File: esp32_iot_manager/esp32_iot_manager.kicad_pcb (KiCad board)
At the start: 4 copper layers, 76.5 x 58 mm, 88 parts, among them J1 SS-52400-002, J2 B2B-PH-SM4-TB, J3 GSD090012SEU, J4 Conn_01x04_Pin, J5 Conn_01x05_Pin, Q1 TEMT6000X01, Q2 BC817, Q3 BC817, U1 MCP73871, U2 BME280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

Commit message: 4 layer pcb design done
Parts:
- moved LED4 7.12 mm to (160.0, 54.9)
- moved R10 7.12 mm to (160.0, 51.1)
- moved U5 4.82 mm to (171.2, 58.3)
- moved C11 4.54 mm to (170.5, 55.1)
- moved R12 4.54 mm to (168.2, 56.9)
- moved R13 4.54 mm to (168.2, 53.3)
- moved TP1 2.50 mm to (193.0, 62.5)
- moved TP2 1.52 mm to (193.0, 66.5)
- moved TP5 1.50 mm to (193.0, 78.2)
- moved TP3 0.75 mm to (193.0, 70.5)
- moved TP4 0.50 mm to (193.0, 74.5)
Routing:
- added copper zone on In1.Cu, net 3.3V
- added copper zone on In2.Cu, net GND

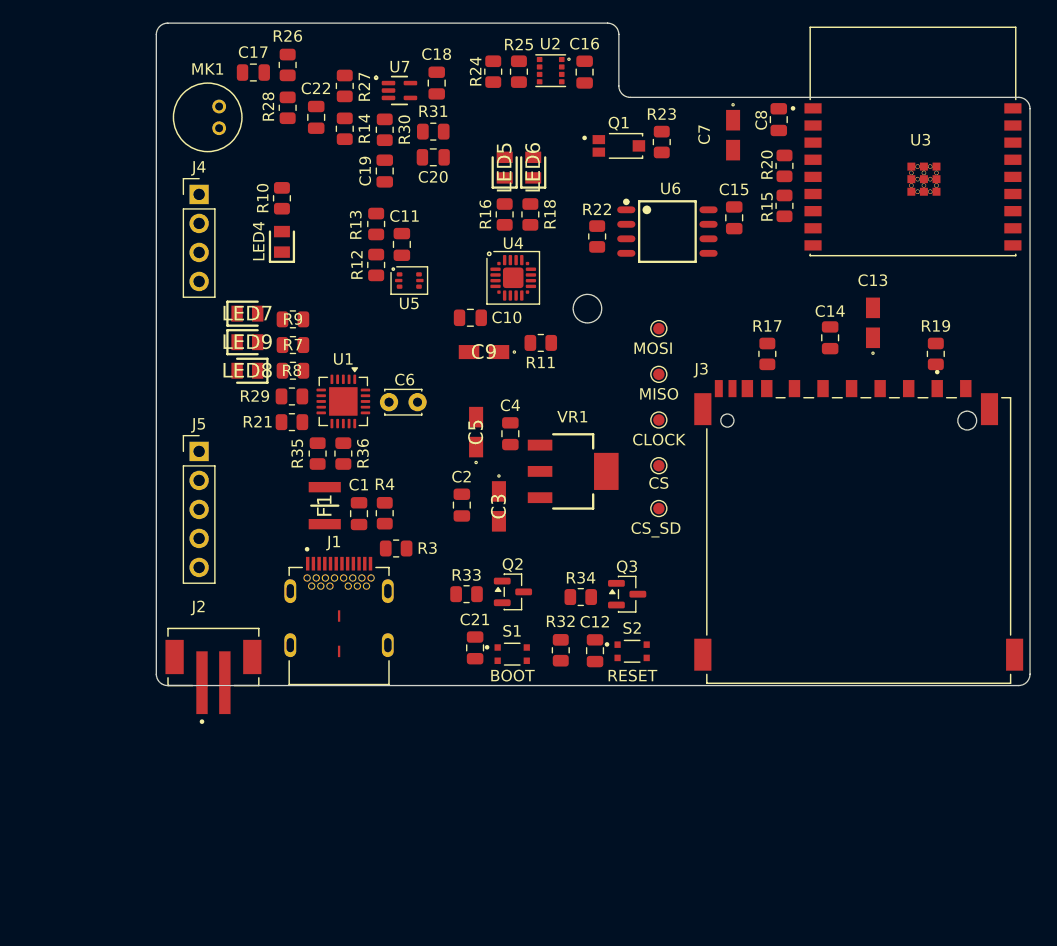
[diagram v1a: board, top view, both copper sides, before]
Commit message: esp32 manager layout
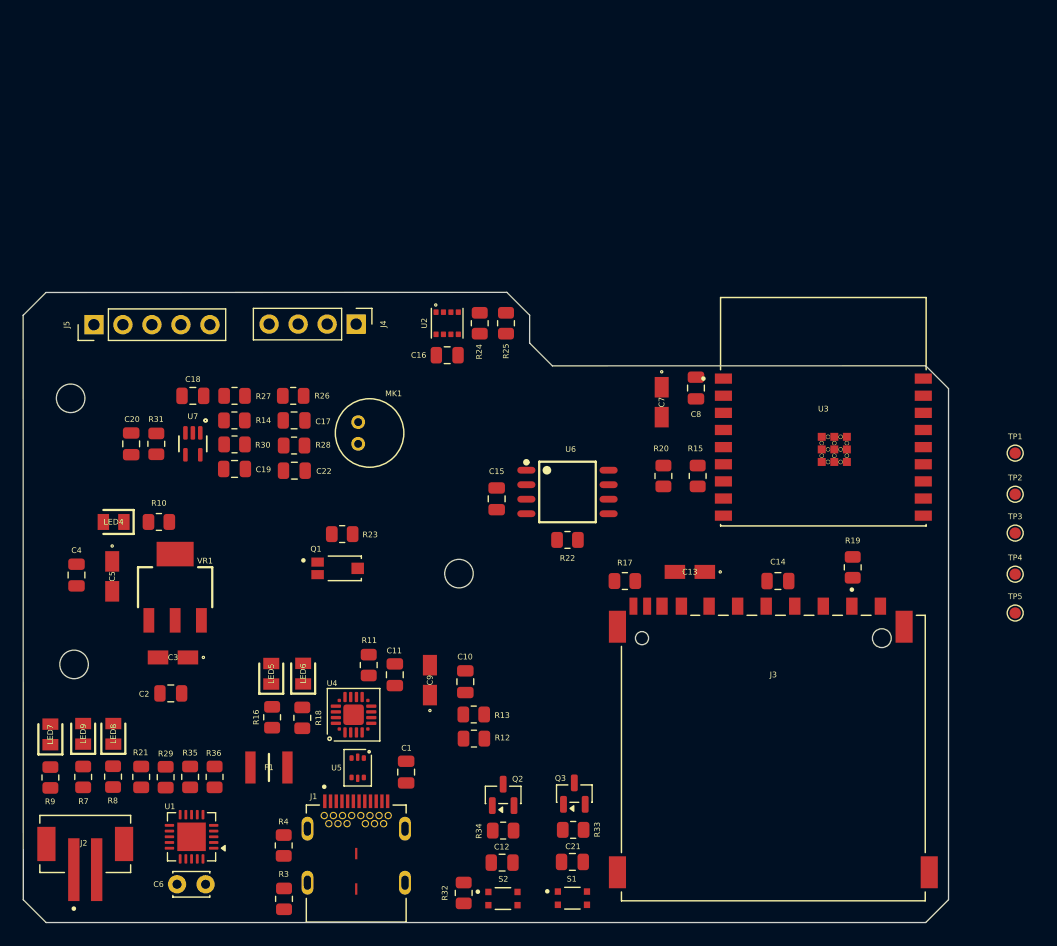
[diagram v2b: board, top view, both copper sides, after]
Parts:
- removed G***: LOGO, JPI_LOGOS:jpi_logo_text_10mm_silkscreen
- removed G***: LOGO, JPI_LOGOS:jpi_logo_10mm_silkscreen
- removed the REF** at (186.8, 60.8)
- added REF**: MountingHole_2.5mm, MountingHole:MountingHole_2.5mm, F.Cu at (141.5, 68.6)
- added REF**: MountingHole_2.5mm, MountingHole:MountingHole_2.5mm, F.Cu at (175.5, 84.0)
- added REF**: MountingHole_2.5mm, MountingHole:MountingHole_2.5mm, F.Cu at (141.8, 91.9)
- S1: value USLPT2819DT2TR -> boot
- S2: value USLPT2819DT2TR -> reset
- TP1: value MOSI -> Test MOSI
- TP2: value MISO -> Test MISO
- TP3: value CLOCK -> Test clock
- TP4: value CS -> Test CS
- TP5: value CS_SD -> Test CS_SD
- U3: value ESP32-C3-WROOM-02-H4 -> ESP32-C3-WROOM-2
- moved LED5 48.8 mm to (159.1, 92.7)
- moved LED6 48.7 mm to (161.9, 92.7)
- moved R16 48.5 mm to (159.1, 96.5)
- moved R18 48.4 mm to (161.8, 96.6), turned to -90 degrees
- moved C6 46.1 mm to (150.8, 111.2)
- moved R9 45.4 mm to (139.7, 101.8), turned to -90 degrees
- moved Q1 44.4 mm to (164.9, 83.5)
- moved R23 44.3 mm to (165.3, 80.5), turned to 180 degrees
- moved R13 43.8 mm to (176.8, 96.3), turned to 0 degrees
- moved U5 42.9 mm to (166.6, 100.9), turned to -90 degrees
- moved R12 42.3 mm to (176.8, 98.4), turned to 0 degrees
- moved R7 42.0 mm to (142.6, 101.8), turned to 90 degrees
- moved U4 40.7 mm to (166.3, 96.3), turned to 90 degrees
- moved LED7 40.7 mm to (139.7, 98.0), turned to 90 degrees
- moved U1 40.4 mm to (152.1, 107.0), turned to 180 degrees
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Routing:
- removed copper zone on In1.Cu, net 3.3V
- removed copper zone on In2.Cu, net GND
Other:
- board size 76.5 x 58 mm -> 81 x 55.2 mm
- board text removed: "BOOT"
- board text removed: "ESP32 IOT MANAGER V1 Jose Padilla 2025"
- board text removed: "RESET"

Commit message: copper zones 1
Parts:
- moved C1 0.15 mm to (170.8, 101.2), turned to -90 degrees
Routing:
- added copper zone on In1.Cu, net /+5V_USB
- added copper zone on In1.Cu, net /VBUS
- added copper zone on In1.Cu, net 3.3V
- added copper zone on In2.Cu, net GND
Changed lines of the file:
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@@
 	)
 	(footprint "MountingHole:MountingHole_2.5mm"
+		(locked yes)
 		(layer "F.Cu")
 		(at 141.5 68.6)
@@
 	)
 	(footprint "Capacitor_SMD:C_0805_2012Metric"
+		(locked yes)
 		(layer "F.Cu")
 		(at 178.8 77.4 90)
@@
 	)
 	(footprint "MountingHole:MountingHole_2.5mm"
+		(locked yes)
 		(layer "F.Cu")
 		(at 175.5 83.95)
@@
 		(locked yes)
 		(layer "F.Cu")
-		(at 170.8742 101.3284 90)
+		(at 170.75 101.25 -90)
 		(descr "Capacitor SMD 0805 (2012 Metric), square (rectangular) end terminal, IPC-7351 nominal, (Body size source: IPC-SM-782 page 76, https://www.pcb-3d.com/wordpress/wp-content/uploads/ipc-sm-782a_amendment_1_and_2.pdf, https://docs.google.com/spreadsheets/d/1BsfQQcO9C6DZCsRaXUlFlo91Tg2WpOkGARC1WS5S8t0/edit?usp=sharing), generated with kicad-footprint-generator")
 		(tags "capacitor")
 		(property "Reference" "C1"
-			(at 2.1082 0.0254 180)
+			(at 0.05 -1.5 0)
 			(layer "F.SilkS")
 			(effects
@@
 		(attr smd)
 		(fp_line
-			(start -0.261252 -0.735)
-			(end 0.261252 -0.735)
+			(start -0.261252 0.735)
+			(end 0.261252 0.735)
 			(stroke
 				(width 0.12)
@@
 		)
 		(fp_line
-			(start -0.261252 0.735)
-			(end 0.261252 0.735)
+			(start -0.261252 -0.735)
+			(end 0.261252 -0.735)
 			(stroke
 				(width 0.12)
@@
 		)
 		(fp_line
-			(start 1.7 -0.98)
-			(end 1.7 0.98)
+			(start -1.7 0.98)
+			(end -1.7 -0.98)
 			(stroke
 				(width 0.05)
@@
 		)
 		(fp_line
-			(start -1.7 -0.98)
-			(end 1.7 -0.98)
+			(start 1.7 0.98)
+			(end -1.7 0.98)
 			(stroke
 				(width 0.05)
@@
 		)
 		(fp_line
-			(start 1.7 0.98)
-			(end -1.7 0.98)
+			(start -1.7 -0.98)
+			(end 1.7 -0.98)
 			(stroke
 				(width 0.05)
@@
 		)
 		(fp_line
-			(start -1.7 0.98)
-			(end -1.7 -0.98)
+			(start 1.7 -0.98)
+			(end 1.7 0.98)
 			(stroke
 				(width 0.05)
@@
 		)
 		(fp_line
-			(start 1 -0.625)
-			(end 1 0.625)
+			(start -1 0.625)
+			(end -1 -0.625)
 			(stroke
 				(width 0.1)
@@
 		)
 		(fp_line
-			(start -1 -0.625)
-			(end 1 -0.625)
+			(start 1 0.625)
+			(end -1 0.625)
 			(stroke
 				(width 0.1)
@@
 		)
 		(fp_line
-			(start 1 0.625)
-			(end -1 0.625)
+			(start -1 -0.625)
+			(end 1 -0.625)
 			(stroke
 				(width 0.1)
@@
 		)
 		(fp_line
-			(start -1 0.625)
-			(end -1 -0.625)
+			(start 1 -0.625)
+			(end 1 0.625)
 			(stroke
 				(width 0.1)
@@
 		)
 		(pad "1" smd roundrect
-			(at -0.95 0 90)
+			(at -0.95 0 270)
 			(size 1 1.45)
 			(layers "F.Cu" "F.Mask" "F.Paste")
@@
 		)
 		(pad "2" smd roundrect
-			(at 0.95 0 90)
+			(at 0.95 0 270)
 			(size 1 1.45)
 			(layers "F.Cu" "F.Mask" "F.Paste")
@@
 	)
 	(footprint "Resistor_SMD:R_0805_2012Metric"
+		(locked yes)
 		(layer "F.Cu")
 		(at 185 81)
@@
 	)
 	(footprint "esp32_manager_project:SOIC127P790X216-8N"
+		(locked yes)
 		(layer "F.Cu")
 		(at 185 76.8)
@@
 	)
 	(footprint "MountingHole:MountingHole_2.5mm"
+		(locked yes)
 		(layer "F.Cu")
 		(at 141.8 91.9)
@@
 		(layer "Edge.Cuts")
 	)
+	(zone
+		(net 2)
+		(net_name "/VBUS")
+		(layer "In1.Cu")
+		(name "VBUS")
+		(hatch edge 0.5)
+		(priority 2)
+		(connect_pads
+			(clearance 0.5)
+		)
+		(min_thickness 0.25)
+		(filled_areas_thickness no)
+		(fill yes
+			(thermal_gap 0.5)
+			(thermal_bridge_width 0.5)
+		)
+		(polygon
+			(pts
+				(xy 158.9278 99.267) (xy 158.95 104.7) (xy 169.85 108.05) (xy 169.77 99.3)
+			)
+		)
+	)
+	(zone
+		(net 5)
+		(net_name "/+5V_USB")
+		(layer "In1.Cu")
+		(name "+5V_USB")
+		(hatch edge 0.5)
+		(priority 3)
+		(connect_pads
+			(clearance 0.5)
+		)
+		(min_thickness 0.25)
+		(filled_areas_thickness no)
+		(fill yes
+			(thermal_gap 0.5)
+			(thermal_bridge_width 0.5)
+		)
+		(polygon
+			(pts
+				(xy 133.85 96.05) (xy 134.6 115.4) (xy 158.8 115.7) (xy 158.761134 99) (xy 146.9 99.303604) (xy 146.9 95.7)
+			)
+		)
+	)
+	(zone
+		(net 4)
+		(net_name "3.3V")
+		(layer "In1.Cu")
+		(name "3.3V")
+		(hatch edge 0.5)
+		(priority 1)
+		(connect_pads
+			(clearance 0.5)
+		)
+		(min_thickness 0.25)
+		(filled_areas_thickness no)
+		(fill yes
+			(thermal_gap 0.5)
+			(thermal_bridge_width 0.5)
+		)
+		(polygon
+			(pts
+				(xy 133.95 57.1) (xy 133.85 95.5) (xy 157.1 95.4172) (xy 157.6 98.75) (xy 174.5 99.347) (xy 174.9634 114.3)
+				(xy 224.7 114.5) (xy 224.5 57)
+			)
+		)
+	)
+	(zone
+		(net 1)
+		(net_name "GND")
+		(layer "In2.Cu")
+		(name "GND")
+		(hatch edge 0.5)
+		(connect_pads
+			(clearance 0.5)
+		)
+		(min_thickness 0.25)
+		(filled_areas_thickness no)
+		(fill yes
+			(thermal_gap 0.5)
+			(thermal_bridge_width 0.5)
+		)
+		(polygon
+			(pts
+				(xy 133.95 57.1) (xy 133.75 116.95) (xy 224.65 116.25) (xy 224.5 57)
+			)
+		)
+	)
 	(group ""
 		(locked yes)
@@
 	(group ""
 		(locked yes)
+		(members "220ccaa6-796a-4d6a-9ab7-883b29717e5c" "249cf918-a966-4327-aa3a-fb72c40c0025"
+			"2a5a075a-f266-40a5-bbce-de782a9f710c" "3d0bf9ac-914c-48b6-829d-3271980821b6"
+			"4fe5ac6c-24eb-4dc5-8fef-4f3ac3acb5dd" "5647cf17-bb07-41b3-935b-b03f06f3fd41"
+			"587a4f05-2035-43cc-aa44-966a9e92decd" "5ffca179-fecc-4ec9-a786-906eb09a7e2f"
+			"6ce5eda7-02ea-4e2b-9759-8416bf550652" "70b23147-223c-4f64-b6a7-e174f641fa7d"
+			"72e9f33d-a3c3-47ec-a8c6-f0c16c201aab" "8063b4f3-c40a-4265-8fe7-c898f112b14e"
+			"82b2164b-5961-4404-b33c-96aba2d5ed5f" "834addef-0716-4498-98ad-62e742affa90"
+			"c0cfe1ac-8287-4501-879f-bbf3132a8faf" "fb90a986-1ab3-47aa-97ff-5b218166a6fc"
+			"fee5394f-792a-4f1a-915a-d9853a453a4f"
+		)
+	)
+	(group ""
+		(locked yes)
 		(members "150d6ae4-9917-4b30-a116-32b07754fa91" "37b22439-2c0a-4a6d-9093-65082881ffc4"
 			"392e1d0e-361d-44f6-9354-56f3f38a05a7" "4089474f-1430-4264-beb6-1f61da944721"
@@
 	)
 	(group ""
+		(locked yes)
 		(members "34644797-ae92-45a9-8e81-adda4853b222" "9d8898de-a6d6-404c-bc84-002f5991435e"
 			"b7de1be1-d8c5-4341-aeb1-c33dc0af0f15"
@@
 		)
 	)
-	(group ""
-		(locked yes)
-		(members "220ccaa6-796a-4d6a-9ab7-883b29717e5c" "249cf918-a966-4327-aa3a-fb72c40c0025"
-			"2a5a075a-f266-40a5-bbce-de782a9f710c" "3d0bf9ac-914c-48b6-829d-3271980821b6"
-			"4fe5ac6c-24eb-4dc5-8fef-4f3ac3acb5dd" "5647cf17-bb07-41b3-935b-b03f06f3fd41"
-			"587a4f05-2035-43cc-aa44-966a9e92decd" "5ffca179-fecc-4ec9-a786-906eb09a7e2f"
-			"6ce5eda7-02ea-4e2b-9759-8416bf550652" "70b23147-223c-4f64-b6a7-e174f641fa7d"
-			"72e9f33d-a3c3-47ec-a8c6-f0c16c201aab" "8063b4f3-c40a-4265-8fe7-c898f112b14e"
-			"82b2164b-5961-4404-b33c-96aba2d5ed5f" "834addef-0716-4498-98ad-62e742affa90"
-			"c0cfe1ac-8287-4501-879f-bbf3132a8faf" "fb90a986-1ab3-47aa-97ff-5b218166a6fc"
-			"fee5394f-792a-4f1a-915a-d9853a453a4f"
-		)
-	)

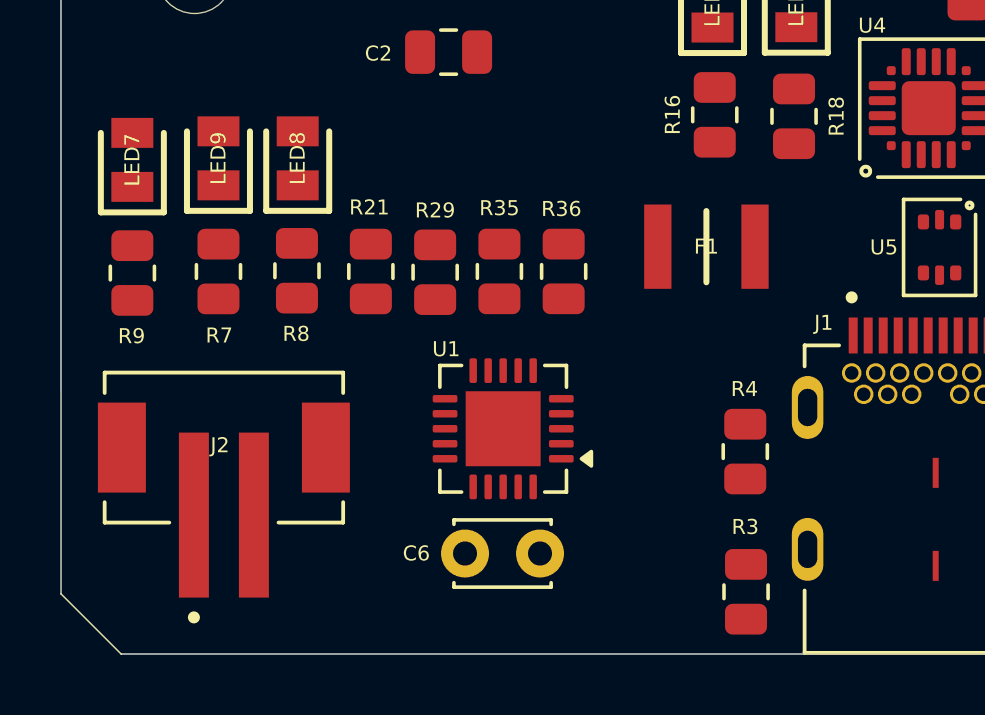
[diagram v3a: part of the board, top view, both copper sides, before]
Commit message: copper zones
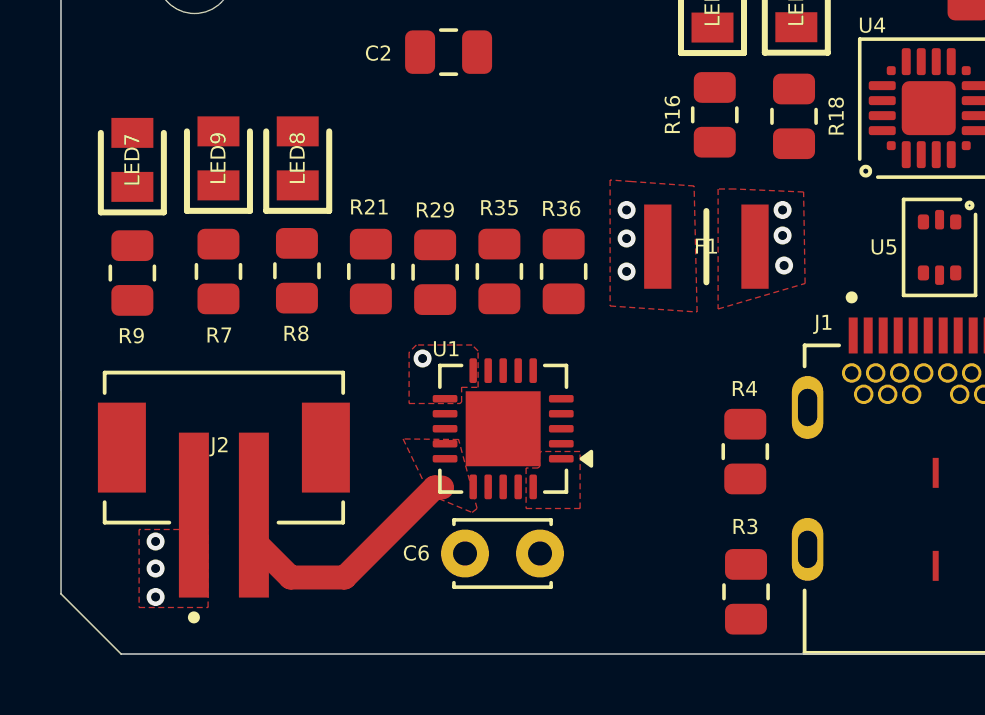
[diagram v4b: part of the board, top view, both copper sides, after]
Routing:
- net /VBAT: track 0.00 -> 10.0 mm
- net GND: vias 0 -> 4
- net /VBUS: vias 0 -> 3
- net /+5V_USB: vias 0 -> 3
- added copper zone on F.Cu, net +5V
- added copper zone on F.Cu, net /+5V_USB
- added copper zone on F.Cu, net /VBAT
- added copper zone on F.Cu, net /VBUS
- added copper zone on F.Cu, net GND

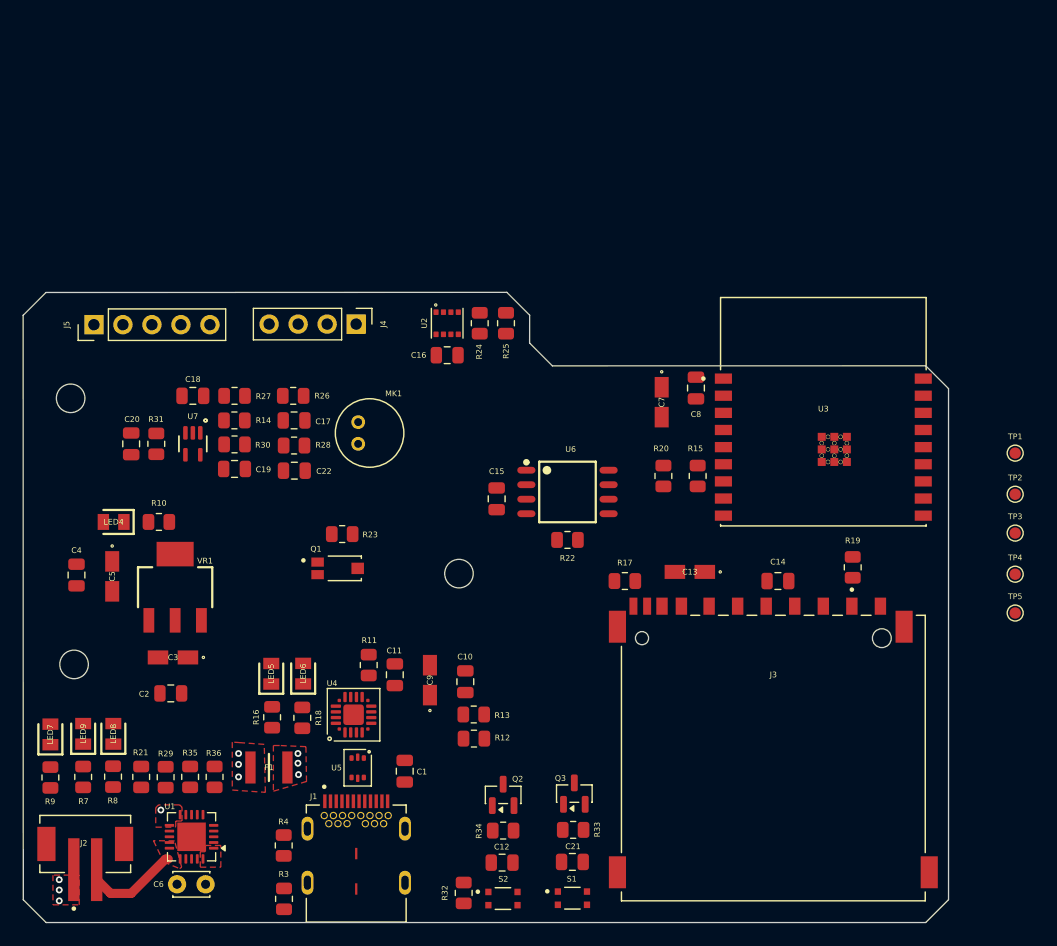
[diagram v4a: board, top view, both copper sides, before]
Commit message: added 3.3v testpoint, routed diff pairs
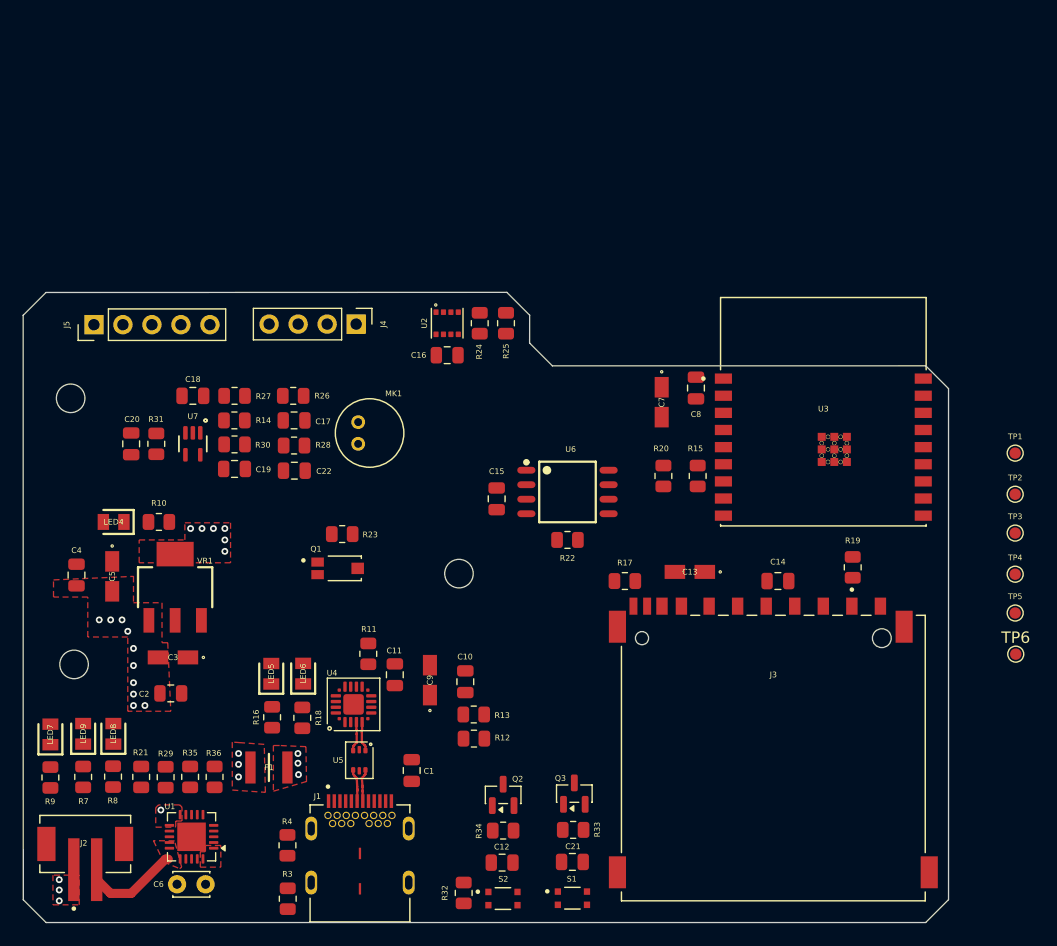
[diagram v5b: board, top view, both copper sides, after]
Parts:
- added TP6: Test 3.3V, TestPoint:TestPoint_Pad_D1.0mm, F.Cu at (224.2, 91.0)
- S1: value boot -> USLPT2819DT2TR
- S2: value reset -> USLPT2819DT2TR
- U3: value ESP32-C3-WROOM-2 -> ESP32-C3-WROOM-02-H4
- moved R11 0.98 mm to (167.6, 91.0)
- moved U4 0.90 mm to (166.3, 95.4)
- moved U5 0.67 mm to (166.8, 100.3)
- moved C1 0.61 mm to (171.4, 101.2)
- moved J1 0.33 mm to (166.8, 111.0)
- moved R3 0.33 mm to (160.5, 112.4)
- moved R4 0.33 mm to (160.5, 107.7)
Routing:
- net /USB_DP: track 0.00 -> 3.00 mm
- net /USB_DN: track 0.00 -> 2.87 mm
- net /ESP32-C3-02/USB_DATA+: track 0.00 -> 2.64 mm
- net /ESP32-C3-02/USB_DATA-: track 0.00 -> 2.64 mm
- net GND: vias 4 -> 14
- net 3.3V: vias 0 -> 6
- added copper zone on F.Cu, net 3.3V
